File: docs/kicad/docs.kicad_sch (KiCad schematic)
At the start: 16 parts, among them SW1 SW_PUSH, SW2 SW_PUSH, SW3 SW_PUSH, SW4 SW_PUSH, SW5 SW_PUSH, SW6 SW_PUSH, SW7 RotaryEncoder_Switch, U1 Pico, U2 LCD

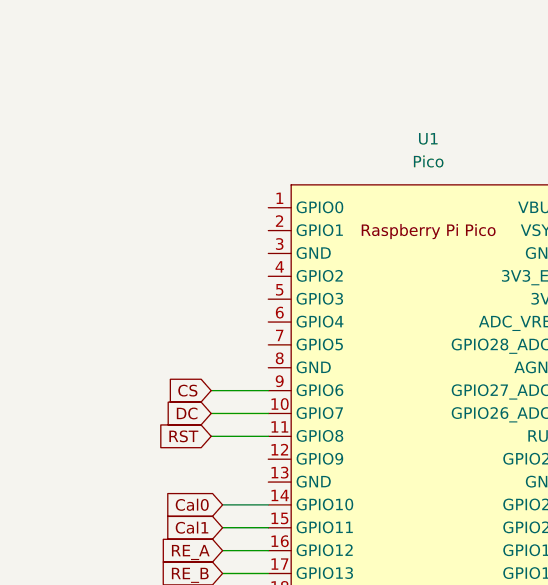
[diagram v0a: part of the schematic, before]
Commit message: 回路図にLEDを追加
KiCadの回路図にLEDを追加
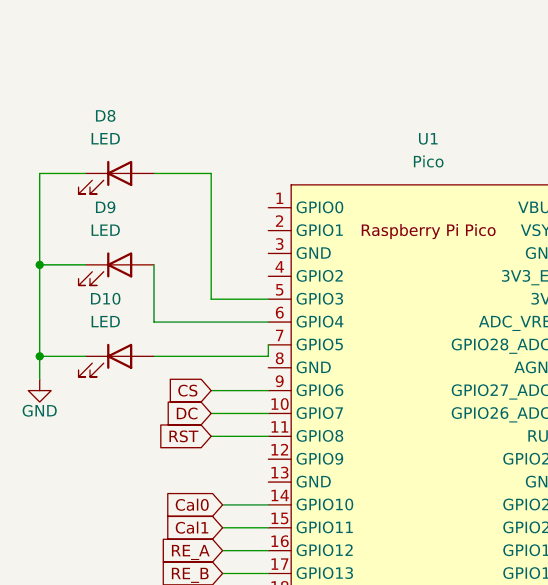
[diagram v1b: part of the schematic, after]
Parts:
- added D10, D8, D9: LED, symbol Device:LED
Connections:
- net GND: now also D10.1 (K), D8.1 (K), D9.1 (K)
- net at U1.5 (GPIO3): now also D8.2 (A)
- net at U1.6 (GPIO4): now also D9.2 (A)
- net at U1.7 (GPIO5): now also D10.2 (A)
